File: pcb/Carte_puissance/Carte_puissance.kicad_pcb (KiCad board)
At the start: 2 copper layers, 118.3 x 60 mm, 0 parts

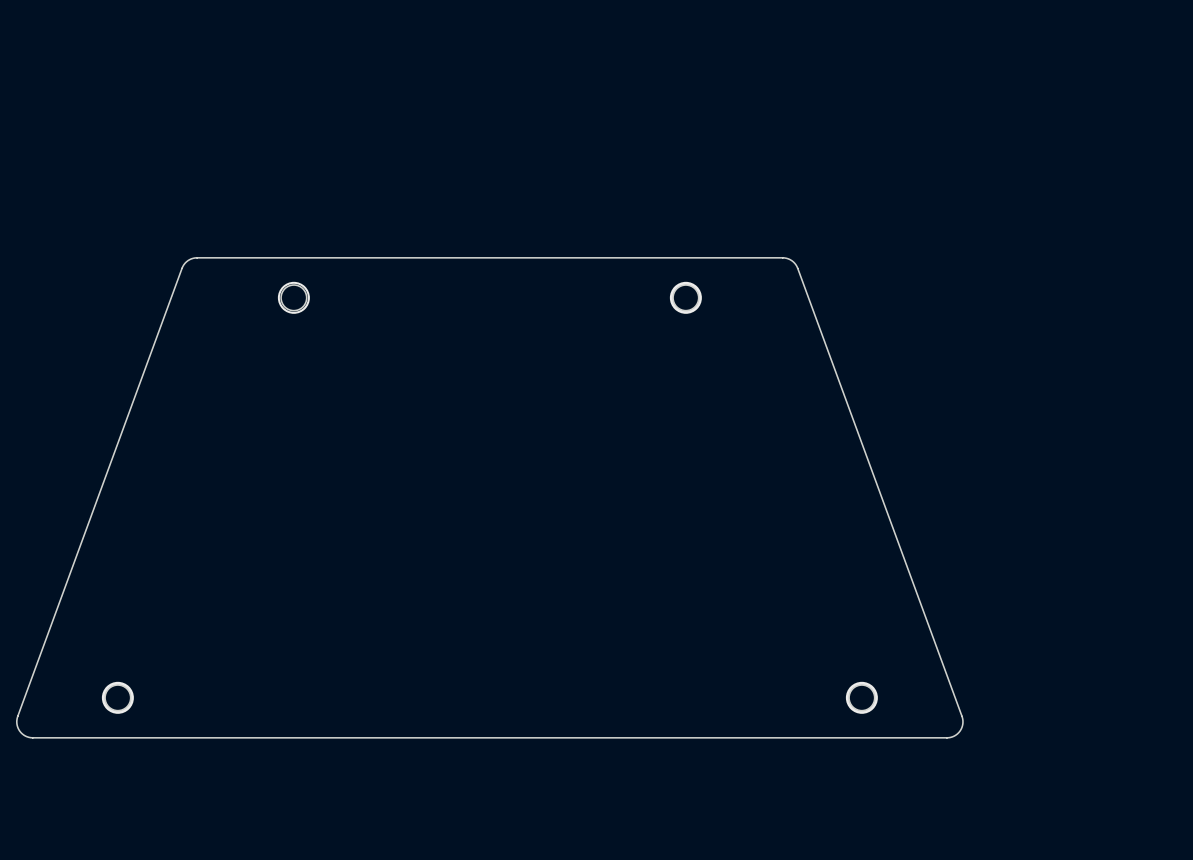
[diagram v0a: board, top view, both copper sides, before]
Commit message: Essai de Freecad, pas concluant
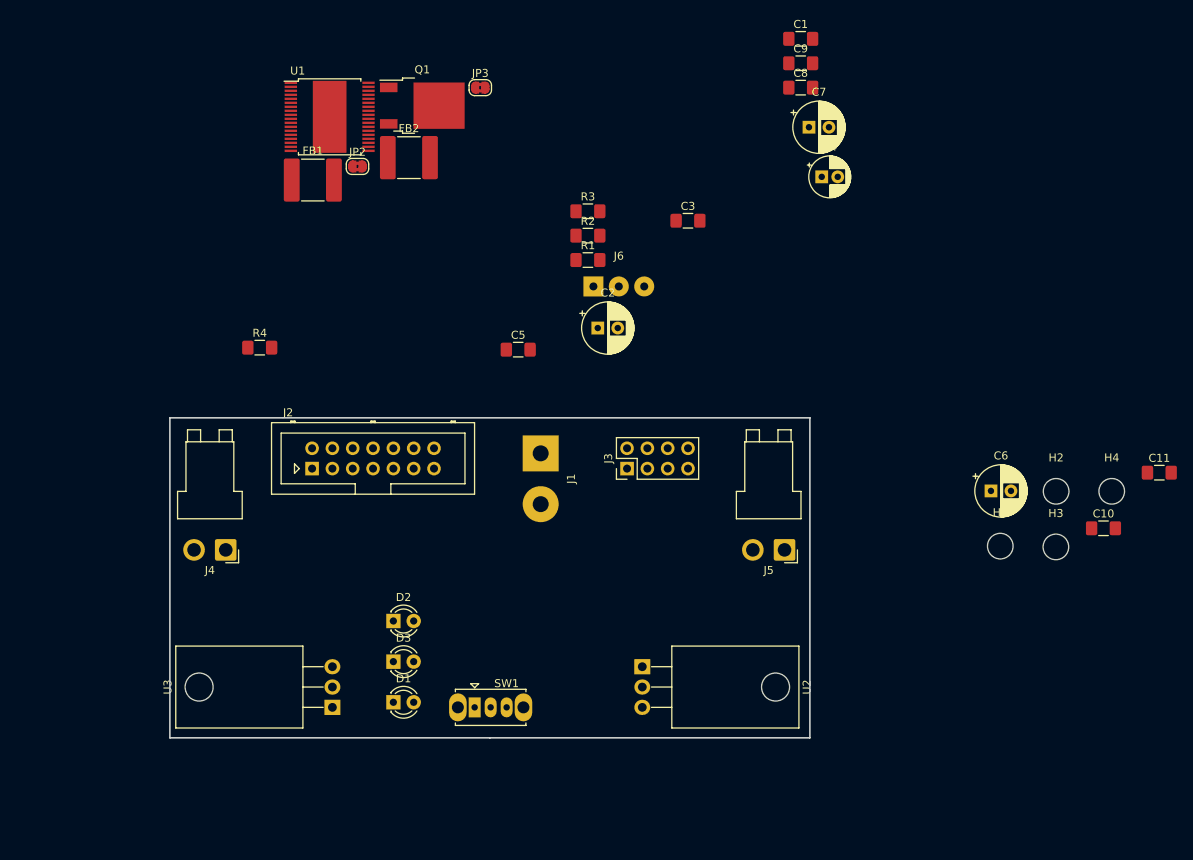
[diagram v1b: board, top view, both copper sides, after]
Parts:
- added C1: 100nF, Capacitor_SMD:C_1206_3216Metric_Pad1.42x1.75mm_HandSolder, F.Cu at (194.8, 38.0)
- added C10: 100nF, Capacitor_SMD:C_1206_3216Metric_Pad1.42x1.75mm_HandSolder, F.Cu at (232.7, 99.2)
- added C11: 100nF, Capacitor_SMD:C_1206_3216Metric_Pad1.42x1.75mm_HandSolder, F.Cu at (239.7, 92.2)
- added C2: 100µF, Capacitor_THT:CP_Radial_D6.3mm_P2.50mm, F.Cu at (169.5, 74.1)
- added C3: 100nF, Capacitor_SMD:C_1206_3216Metric_Pad1.42x1.75mm_HandSolder, F.Cu at (180.7, 60.7)
- added C4: 10µF, Capacitor_THT:CP_Radial_D5.0mm_P2.00mm, F.Cu at (197.5, 55.2)
- added C5: 100nF, Capacitor_SMD:C_1206_3216Metric_Pad1.42x1.75mm_HandSolder, F.Cu at (159.5, 76.8)
- added C6: 100µF, Capacitor_THT:CP_Radial_D6.3mm_P2.50mm, F.Cu at (218.6, 94.5)
- added C7: 100µF, Capacitor_THT:CP_Radial_D6.3mm_P2.50mm, F.Cu at (195.9, 49.0)
- added C8: 100nF, Capacitor_SMD:C_1206_3216Metric_Pad1.42x1.75mm_HandSolder, F.Cu at (194.8, 44.1)
- added C9: 100nF, Capacitor_SMD:C_1206_3216Metric_Pad1.42x1.75mm_HandSolder, F.Cu at (194.8, 41.0)
- added D1: LED, LED_THT:LED_D3.0mm, F.Cu at (143.9, 120.9)
- added D2: LED, LED_THT:LED_D3.0mm, F.Cu at (143.9, 110.8)
- added D3: LED, LED_THT:LED_D3.0mm, F.Cu at (143.9, 115.8)
- added FB1: Ferrite_Bead, Capacitor_SMD:C_2220_5650Metric_Pad1.97x5.40mm_HandSolder, F.Cu at (133.9, 55.6)
- added FB2: Ferrite_Bead, Capacitor_SMD:C_2220_5650Metric_Pad1.97x5.40mm_HandSolder, F.Cu at (145.9, 52.8)
- added H1: MountingHole, MountingHole:MountingHole_3.2mm_M3, F.Cu at (219.8, 101.4)
- added H2: MountingHole, MountingHole:MountingHole_3.2mm_M3, F.Cu at (226.8, 94.5)
- added H3: MountingHole, MountingHole:MountingHole_3.2mm_M3, F.Cu at (226.7, 101.5)
- added H4: MountingHole, MountingHole:MountingHole_3.2mm_M3, F.Cu at (233.7, 94.5)
- added J1: Conn_01x02, Connector_Wire:SolderWirePad_1x02_P7.62mm_Drill2mm, F.Cu at (162.3, 89.8)
- added J2: Conn_02x07_Odd_Even, Connector_Multicomp:Multicomp_MC9A12-1434_2x07_P2.54mm_Vertical, F.Cu at (133.8, 91.7)
- added J3: Conn_02x04_Odd_Even, Connector_PinHeader_2.54mm:PinHeader_2x04_P2.54mm_Vertical, F.Cu at (173.1, 91.7)
- added J4: MOT LEFT, Connector_JST:JST_VH_B2PS-VH_1x02_P3.96mm_Horizontal, F.Cu at (123.0, 101.9)
- added J5: MOT RIGHT, Connector_JST:JST_VH_B2PS-VH_1x02_P3.96mm_Horizontal, F.Cu at (192.8, 101.9)
- added J6: Conn_01x03, Connector_Wire:SolderWirePad_1x03_P3.175mm_Drill1mm, F.Cu at (168.9, 68.9)
- added JP2: SolderJumper_2_Bridged, Jumper:SolderJumper-2_P1.3mm_Bridged2Bar_RoundedPad1.0x1.5mm, F.Cu at (139.4, 53.9)
- added JP3: SolderJumper_2_Bridged, Jumper:SolderJumper-2_P1.3mm_Bridged2Bar_RoundedPad1.0x1.5mm, F.Cu at (154.8, 44.1)
- added Q1: IPD50P04P4-13, Package_TO_SOT_SMD:TO-252-2, F.Cu at (147.5, 46.3)
- added R1: 10K, Resistor_SMD:R_1206_3216Metric_Pad1.42x1.75mm_HandSolder, F.Cu at (168.2, 65.6)
- added R2: 330R, Resistor_SMD:R_1206_3216Metric_Pad1.42x1.75mm_HandSolder, F.Cu at (168.2, 62.6)
- added R3: 330R, Resistor_SMD:R_1206_3216Metric_Pad1.42x1.75mm_HandSolder, F.Cu at (168.2, 59.5)
- added R4: 330R, Resistor_SMD:R_1206_3216Metric_Pad1.42x1.75mm_HandSolder, F.Cu at (127.2, 76.6)
- added SW1: SW_SPDT, Button_Switch_THT:SW_Slide_1P2T_CK_OS102011MS2Q, F.Cu at (154.1, 121.5)
- added U1: IFX9202ED, Insa:Infineon_PG_DSO_36, F.Cu at (136.0, 47.7)
- added U2: MIC29500-3.3WT, Package_TO_SOT_THT:TO-220-3_Horizontal_TabDown, F.Cu at (175.0, 116.5)
- added U3: MIC29500-5.0WT, Package_TO_SOT_THT:TO-220-3_Horizontal_TabDown, F.Cu at (136.3, 121.5)
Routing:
- net (no net): vias 4 -> 0
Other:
- board size 118.3 x 60 mm -> 80 x 40 mm

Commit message: Cartes En cours de conception
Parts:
- FB1, FB2: footprint Capacitor_SMD:C_2220_5650Metric_Pad1.97x5.40mm_HandSolder -> Capacitor_SMD:C_1812_4532Metric_Pad1.30x3.40mm_HandSolder
- J3: value Conn_02x04_Odd_Even -> Molex KK 254; footprint Connector_PinHeader_2.54mm:PinHeader_2x04_P2.54mm_Vertical -> Connector_Molex:Molex_KK-254_AE-6410-04A_1x04_P2.54mm_Vertical
- moved H3 106.4 mm to (125.1, 132.9)
- moved H2 101.7 mm to (125.1, 97.9)
- moved JP3 81.2 mm to (164.3, 124.7)
- moved Q1 81.2 mm to (157.1, 127.0)
- moved U1 65.1 mm to (156.6, 109.5)
- moved J6 61.4 mm to (136.3, 120.9), turned to 90 degrees
- moved C10 60.4 mm to (173.6, 111.9)
- moved C11 60.4 mm to (180.6, 104.9)
- moved R1 58.7 mm to (146.6, 120.2)
- moved R2 58.7 mm to (146.6, 117.2)
- moved R3 58.7 mm to (146.6, 114.1)
- moved FB1 50.9 mm to (158.6, 100.1)
- moved FB2 50.9 mm to (170.6, 97.3)
- moved JP2 50.9 mm to (164.2, 98.4)
- moved C1 47.0 mm to (196.7, 85.0)
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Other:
- board size 80 x 40 mm -> 114 x 57 mm

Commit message: demarrage carte capteurs
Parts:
- removed C6, C7: 100µF, Capacitor_THT:CP_Radial_D6.3mm_P2.50mm
- removed H1, H3: MountingHole, MountingHole:MountingHole_3.2mm_M3
- removed U1: IFX9202ED, Insa:Infineon_PG_DSO_36
- added C12: 1nF, Capacitor_SMD:C_1206_3216Metric_Pad1.42x1.75mm_HandSolder, F.Cu at (143.3, 103.1)
- added C13: 100nF, Capacitor_SMD:C_1206_3216Metric_Pad1.42x1.75mm_HandSolder, F.Cu at (143.3, 105.7)
- added C14: 100nF, Capacitor_SMD:C_1206_3216Metric_Pad1.42x1.75mm_HandSolder, F.Cu at (138.8, 90.4)
- added C15: 1nF, Capacitor_SMD:C_1206_3216Metric_Pad1.42x1.75mm_HandSolder, F.Cu at (175.3, 93.0)
- added C16: 100nF, Capacitor_SMD:C_1206_3216Metric_Pad1.42x1.75mm_HandSolder, F.Cu at (175.3, 90.4)
- added C17: 100nF, Capacitor_SMD:C_1206_3216Metric_Pad1.42x1.75mm_HandSolder, F.Cu at (175.0, 113.9)
- added C19: 100nF, Capacitor_SMD:C_1206_3216Metric_Pad1.42x1.75mm_HandSolder, F.Cu at (132.5, 97.4)
- added C20: 470µF, Capacitor_THT:CP_Radial_D6.3mm_P2.50mm, F.Cu at (138.2, 98.7)
- added C22: 100nF, Capacitor_SMD:C_1206_3216Metric_Pad1.42x1.75mm_HandSolder, F.Cu at (174.4, 98.7)
- added C23: 470µF, Capacitor_THT:CP_Radial_D6.3mm_P2.50mm, F.Cu at (179.5, 100.0)
- added Logo_1: LOGO, Insa:insa-image, F.Cu at (136.2, 116.2)
- added Logo_3: WEEE-Logo_4.2x6mm_SilkScreen, Symbol:WEEE-Logo_4.2x6mm_SilkScreen, B.Cu at (184.9, 107.1)
- added Logo_4: ESD-Logo_6.6x6mm_SilkScreen, Symbol:ESD-Logo_6.6x6mm_SilkScreen, F.Cu at (145.8, 85.7)
- added Q2: BTN8982TA, Package_TO_SOT_SMD:TO-263-7_TabPin8, F.Cu at (119.8, 87.3)
- added Q3: BTN8982TA, Package_TO_SOT_SMD:TO-263-7_TabPin8, F.Cu at (125.5, 108.2)
- added Q4: BTN8982TA, Package_TO_SOT_SMD:TO-263-7_TabPin8, F.Cu at (187.7, 108.2)
- added Q5: BTN8982TA, Package_TO_SOT_SMD:TO-263-7_TabPin8, F.Cu at (194.1, 87.3)
- added R10: 10K, Resistor_SMD:R_1206_3216Metric_Pad1.42x1.75mm_HandSolder, F.Cu at (132.5, 91.7)
- added R11: 10K, Resistor_SMD:R_1206_3216Metric_Pad1.42x1.75mm_HandSolder, F.Cu at (175.3, 87.3)
- added R12: 10K, Resistor_SMD:R_1206_3216Metric_Pad1.42x1.75mm_HandSolder, F.Cu at (175.0, 105.7)
- added R13: 1K, Resistor_SMD:R_1206_3216Metric_Pad1.42x1.75mm_HandSolder, F.Cu at (137.6, 103.1)
- added R14: 510R, Resistor_SMD:R_1206_3216Metric_Pad1.42x1.75mm_HandSolder, F.Cu at (137.6, 105.7)
- added R15: 510R, Resistor_SMD:R_1206_3216Metric_Pad1.42x1.75mm_HandSolder, F.Cu at (136.3, 90.4)
- added R16: 1K, Resistor_SMD:R_1206_3216Metric_Pad1.42x1.75mm_HandSolder, F.Cu at (180.8, 93.0)
- added R17: 510R, Resistor_SMD:R_1206_3216Metric_Pad1.42x1.75mm_HandSolder, F.Cu at (180.8, 90.4)
- added R18: 510R, Resistor_SMD:R_1206_3216Metric_Pad1.42x1.75mm_HandSolder, F.Cu at (175.0, 111.4)
- added R5: 10K, Resistor_SMD:R_1206_3216Metric_Pad1.42x1.75mm_HandSolder, F.Cu at (137.6, 108.8)
- added R6: 10K, Resistor_SMD:R_1206_3216Metric_Pad1.42x1.75mm_HandSolder, F.Cu at (132.5, 89.2)
- added R7: 10K, Resistor_SMD:R_1206_3216Metric_Pad1.42x1.75mm_HandSolder, F.Cu at (180.8, 87.3)
- added R8: 10K, Resistor_SMD:R_1206_3216Metric_Pad1.42x1.75mm_HandSolder, F.Cu at (175.0, 108.2)
- added R9: 10K, Resistor_SMD:R_1206_3216Metric_Pad1.42x1.75mm_HandSolder, F.Cu at (137.6, 111.4)
- added REF**: OSHW-Logo2_14.6x12mm_SilkScreen, Symbol:OSHW-Logo2_14.6x12mm_SilkScreen, B.Cu at (131.1, 107.6)
- C1, C5: value 100nF -> 100µF; footprint Capacitor_SMD:C_1206_3216Metric_Pad1.42x1.75mm_HandSolder -> Capacitor_THT:CP_Radial_D6.3mm_P2.50mm
- C2: value 100µF -> 100nF; footprint Capacitor_THT:CP_Radial_D6.3mm_P2.50mm -> Capacitor_SMD:C_1206_3216Metric_Pad1.42x1.75mm_HandSolder
- C3: value 100nF -> 10µF; footprint Capacitor_SMD:C_1206_3216Metric_Pad1.42x1.75mm_HandSolder -> Capacitor_THT:CP_Radial_D5.0mm_P2.00mm
- C4: value 10µF -> 100nF; footprint Capacitor_THT:CP_Radial_D5.0mm_P2.00mm -> Capacitor_SMD:C_1206_3216Metric_Pad1.42x1.75mm_HandSolder
- JP2, JP3: moved to B.Cu
- moved C9 95.2 mm to (102.6, 102.5), turned to 270 degrees
- moved C8 91.0 mm to (106.5, 102.5), turned to 90 degrees
- moved C4 62.4 mm to (145.8, 134.2), turned to 90 degrees
- moved FB2 49.3 mm to (128.0, 122.2), turned to 90 degrees
- moved C1 48.4 mm to (167.4, 123.5), turned to 180 degrees
- moved C2 46.3 mm to (166.1, 129.2), turned to 180 degrees
- moved C5 44.2 mm to (135.0, 120.9), turned to 270 degrees
- moved C3 42.8 mm to (166.1, 134.9), turned to 90 degrees
- moved C10 38.1 mm to (210.6, 102.5), turned to 90 degrees
- moved JP2 37.1 mm to (177.6, 133.0), turned to 180 degrees
- moved R4 34.4 mm to (153.4, 129.2)
- moved Q1 33.4 mm to (158.5, 93.6)
- moved J2 30.5 mm to (149.6, 115.2)
- moved JP3 29.8 mm to (135.7, 133.0), turned to 180 degrees
- moved FB1 27.5 mm to (173.1, 123.5), turned to 90 degrees
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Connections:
- C1 pad 1: Net-(C1-Pad1) -> VCC
- C1 pad 2: Net-(C1-Pad2) -> GND
- C2 pad 1: Net-(C1-Pad1) -> VCC
- C2 pad 2: Net-(C1-Pad2) -> GND
- C3 pad 1: VCC -> +3V3
- C4 pad 1: +3V3 -> Net-(C4-Pad1)
- C4 pad 2: GND -> GNDPWR
- C5 pad 1: Net-(C5-Pad1) -> +5V
- C5 pad 2: GNDPWR -> GNDA
- FB2 pad 1: Net-(C5-Pad1) -> Net-(C4-Pad1)
- J2 pad 1: /~CS_SPI_MOT_LEFT -> /DISABLE_MOT_L
- J2 pad 10: /DIR_MOT_R -> /FEEDBACK_MOT_R
- J2 pad 12: /PWM_MOT_L -> /PWM_MOT_R_1
- J2 pad 14: /PWM_MOT_R -> /PWM_MOT_R_2
- J2 pad 3: /SCK_MOT_DRV -> /DISABLE_MOT_R
- J2 pad 4: /~CS_SPI_MOT_RIGHT -> /FEEDBACK_MOT_L
- J2 pad 5: /MOSI_MOT_DRV -> GND
- J2 pad 6: /MISO_MOT_DRV -> /PWM_MOT_L_1
- J2 pad 7: /DISABLE_MOT_L -> GND
- J2 pad 8: /DISABLE_MOT_R -> /PWM_MOT_L_2
- J2 pad 9: /DIR_MOT_L -> GND
- J6 pad 3: GND -> GNDA
- U3 pad 1: Net-(C5-Pad1) -> Net-(C4-Pad1)
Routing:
- net GNDPWR: track 0.00 -> 381.2 mm, vias 0 -> 9
- net +BATT: track 0.00 -> 235.9 mm, vias 0 -> 3
- net GND: track 0.00 -> 159.9 mm, vias 0 -> 1
- net /PWM_MOT_L_2: track 0.00 -> 84.0 mm, vias 0 -> 1
- net /DISABLE_MOT_L: track 0.00 -> 73.1 mm, vias 0 -> 4
- net Net-(J1-Pad2): track 0.00 -> 68.3 mm, vias 0 -> 3
- net Net-(Q1-Pad1): track 0.00 -> 67.3 mm, vias 0 -> 3
- net /FEEDBACK_MOT_R: track 0.00 -> 53.2 mm, vias 0 -> 1
- net /DISABLE_MOT_R: track 0.00 -> 52.6 mm, vias 0 -> 2
- net +3V3: track 0.00 -> 52.4 mm
- net /SERVO_PWM: track 0.00 -> 39.0 mm, vias 0 -> 2
- net GNDA: track 0.00 -> 38.7 mm
- net VCC: track 0.00 -> 37.4 mm
- net /OUT_2_MOT_L: track 0.00 -> 36.8 mm
- net /OUT_1_MOT_R: track 0.00 -> 36.0 mm
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- added copper zone on F.Cu, net +3V3
- added copper zone on F.Cu, net +5V
- added copper zone on B.Cu, net +BATT
- added copper zone on F.Cu, net +BATT
- added copper zone on F.Cu, net /OUT_1_MOT_L
- added copper zone on F.Cu, net /OUT_1_MOT_R
- added copper zone on F.Cu, net /OUT_2_MOT_L
- added copper zone on F.Cu, net /OUT_2_MOT_R
- added copper zone on B.Cu, net GND
- added copper zone on F.Cu, net GND
- added copper zone on B.Cu, net GNDA
- added copper zone on B.Cu, net GNDPWR
- added copper zone on F.Cu, net GNDPWR
- added copper zone on B.Cu, net Net-(J1-Pad2)
- added copper zone on F.Cu, net VCC
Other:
- board text added: "1"
- board text added: "2"

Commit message: Cartes terminées
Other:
- board text added: "+"
- board text added: "-"
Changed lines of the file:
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@@
   (general
     (thickness 1.6)
-    (drawings 24)
+    (drawings 28)
     (tracks 534)
     (zones 0)
@@
     (tags connector)
     (attr virtual)
-    (fp_text reference J1 (at -4.445 0.254 180) (layer F.SilkS)
+    (fp_text reference J1 (at -3.81 -3.175 180) (layer F.SilkS)
       (effects (font (size 1 1) (thickness 0.15)))
     )
@@
       (xy 1.747822 -3.017822)) (layer B.SilkS) (width 0.01))
   )
+  (gr_text - (at 166.146666 84.081) (layer F.SilkS)
+    (effects (font (size 2 2) (thickness 0.2)))
+  )
+  (gr_text + (at 151.541666 84.081) (layer F.SilkS)
+    (effects (font (size 2 2) (thickness 0.2)))
+  )
+  (gr_poly (pts (xy 122.204666 124.086) (xy 122.966666 123.578) (xy 122.966666 124.594)) (layer F.SilkS) (width 0.1))
+  (gr_poly (pts (xy 182.021666 117.228) (xy 181.513666 116.466) (xy 182.529666 116.466)) (layer F.SilkS) (width 0.1))
   (gr_line (start 144.302666 100.464) (end 139.222666 101.48) (layer F.SilkS) (width 0.2))
   (gr_line (start 144.302666 97.924) (end 144.302666 100.464) (layer F.SilkS) (width 0.2))

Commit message: ajout des versions sur les cartes
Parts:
- removed Logo_1: LOGO, Insa:insa-image
- removed Logo_3: WEEE-Logo_4.2x6mm_SilkScreen, Symbol:WEEE-Logo_4.2x6mm_SilkScreen
- removed Logo_4: ESD-Logo_6.6x6mm_SilkScreen, Symbol:ESD-Logo_6.6x6mm_SilkScreen
- removed REF**: OSHW-Logo2_14.6x12mm_SilkScreen, Symbol:OSHW-Logo2_14.6x12mm_SilkScreen
- added C6: 100nF, Capacitor_SMD:C_1206_3216Metric_Pad1.42x1.75mm_HandSolder, F.Cu at (124.2, 124.1)
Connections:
- Q2 pad 6: Net-(Q2-Pad6) -> (no net)
- Q4 pad 6: Net-(Q4-Pad6) -> (no net)
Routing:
- net GNDA: track 38.7 -> 46.2 mm, vias 0 -> 1
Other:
- board text added: "Rev 1A"
- board text added: "Toulouse"

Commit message: leger evolution sur PCB de la carte de puissance
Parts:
- added REF1: OSHW-Logo2_9.8x8mm_SilkScreen, Symbol:OSHW-Logo2_9.8x8mm_SilkScreen, F.Cu at (157.3, 103.1)
- added REF2: LOGO, Insa:insa-image, F.Cu at (144.6, 86.6)
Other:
- board text added: "~Max 10V"
